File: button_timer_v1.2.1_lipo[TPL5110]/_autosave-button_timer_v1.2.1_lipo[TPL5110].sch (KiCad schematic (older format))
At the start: 26 parts, among them J1 Conn_01x05_Female, Q1 TSM2301ACX, SW1 SW_Push, SW2 SW_Push, U1 TPL5110, U2 AP2112K-3.3, X1 ESP-12E

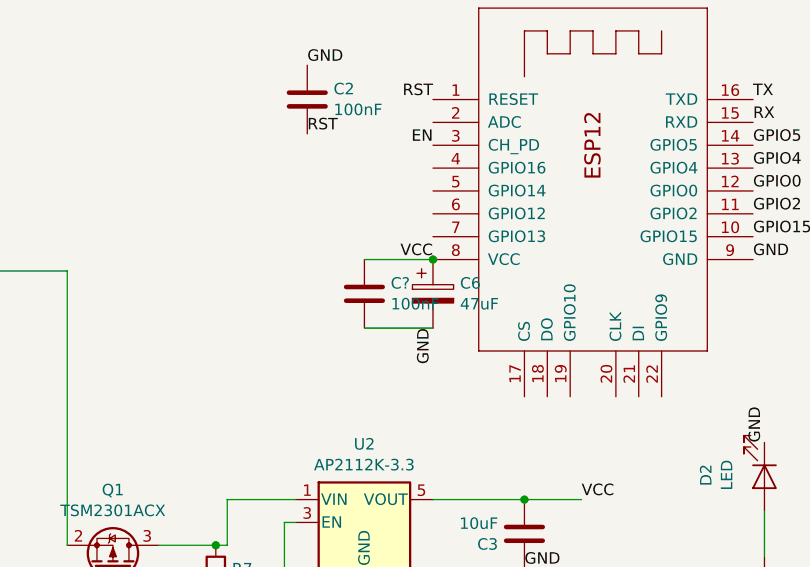
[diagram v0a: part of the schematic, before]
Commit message: Added 100nF decoupling capacitors between VCC and Ground of the ESP
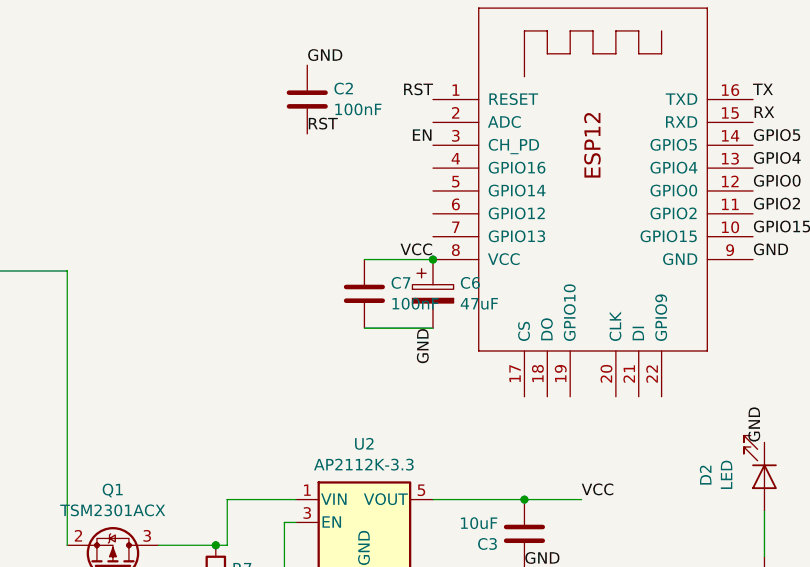
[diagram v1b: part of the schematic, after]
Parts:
- gave numbers to parts that had none: 1
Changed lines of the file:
@@
 GND
 $Comp
-L Device:C C?
+L Device:C C7
 U 1 1 60367D4C
 P 5000 3850
-F 0 "C?" H 5115 3896 50  0000 L CNN
+F 0 "C7" H 5115 3896 50  0000 L CNN
 F 1 "100nF" H 5115 3805 50  0000 L CNN
 F 2 "handsolder:C_0402_1005Metric_Pad0.74x0.62mm_HandSoldermod" H 5038 3700 50  0001 C CNN
